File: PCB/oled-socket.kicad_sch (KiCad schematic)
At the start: 30 parts, among them IC17 TPS6734ID, J5 3-2328724-1

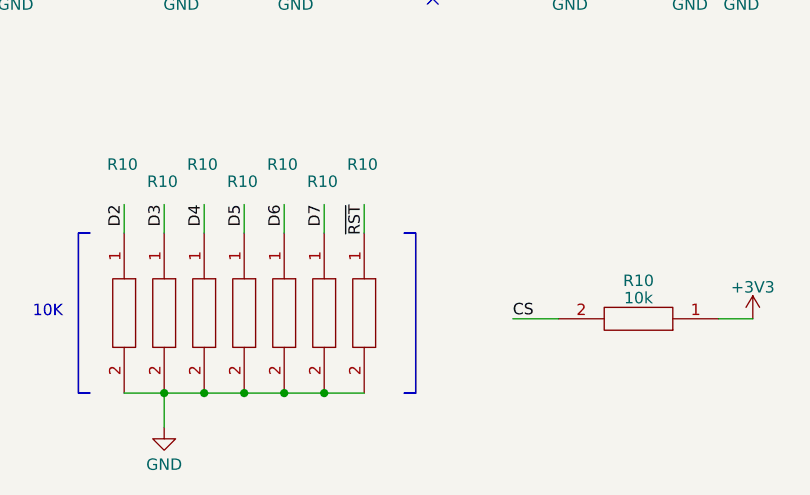
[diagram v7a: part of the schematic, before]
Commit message: redo pinout of entire MCU (closes #34)
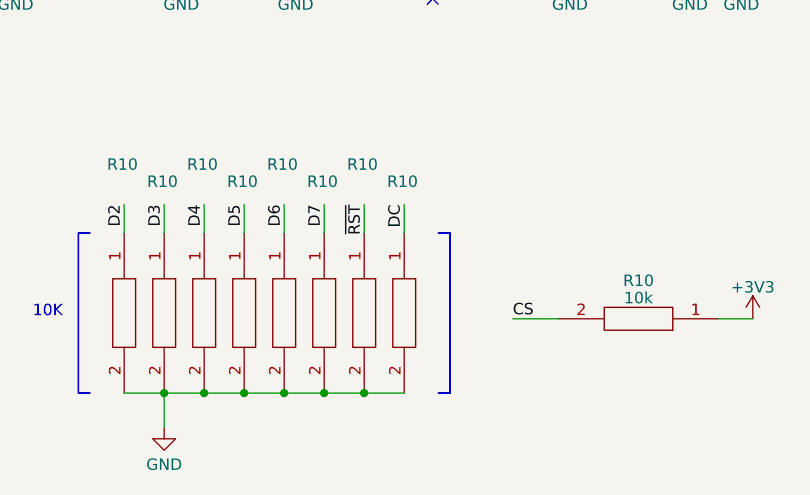
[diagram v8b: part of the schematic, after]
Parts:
- added R10: 10k, RESC1005X40N, symbol SamacSys_Parts:RK73H1ETTP1002F
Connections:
- net DC: now also R10.1
- net GND: now also R10.2
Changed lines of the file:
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@@
     (comment 2 "Joshua Lee Junon")
+  )
+  (junction (at 78.74 174.625) (diameter 0) (color 0 0 0 0)
   )
   (junction (at 65.405 174.625) (diameter 0) (color 0 0 0 0)
@@
     (stroke (width 0) (type default))
   )
+  (wire (pts (xy 83.185 153.67) (xy 83.185 156.845))
+    (stroke (width 0) (type default))
+  )
+  (wire (pts (xy 78.74 174.625) (xy 83.185 174.625))
+    (stroke (width 0) (type default))
+  )
   (wire (pts (xy 69.85 153.67) (xy 69.85 156.845))
     (stroke (width 0) (type default))
@@
     (fill (type none))
   )
-  (rectangle (start 84.455 174.625) (end 84.455 156.845)
+  (rectangle (start 88.265 174.625) (end 88.265 156.845)
     (stroke (width 0) (type default))
     (fill (type none))
   )
-  (rectangle (start 83.185 174.625) (end 84.455 174.625)
+  (rectangle (start 86.995 174.625) (end 88.265 174.625)
     (stroke (width 0) (type default))
     (fill (type none))
   )
-  (rectangle (start 83.185 156.845) (end 84.455 156.845)
+  (rectangle (start 86.995 156.845) (end 88.265 156.845)
     (stroke (width 0) (type default))
     (fill (type none))
@@
   )
   (label "SCK" (at 74.295 45.085 180) (fields_autoplaced)
+    (effects (font (size 1.27 1.27)) (justify right bottom))
+  )
+  (label "DC" (at 83.185 153.67 270) (fields_autoplaced)
     (effects (font (size 1.27 1.27)) (justify right bottom))
   )
@@
         )
       )
+    )
+  )
+  (symbol (lib_id "SamacSys_Parts:RK73H1ETTP1002F") (at 83.185 156.845 270) (unit 1)
+    (in_bom yes) (on_board yes) (dnp no)
+    (property "Reference" "R10" (at 81.28 151.13 90)
+      (effects (font (size 1.27 1.27)) (justify left))
+    )
+    (property "Value" "10k" (at 85.1662 167.0123 90)
+      (effects (font (size 1.27 1.27)) (justify left) hide)
+    )
+    (property "Footprint" "RESC1005X40N" (at 84.455 170.815 0)
+      (effects (font (size 1.27 1.27)) (justify left) hide)
+    )
+    (property "Datasheet" "http://www.koaspeer.com/catimages/Products/RK73-RT/RK73-RT.pdf" (at 81.915 170.815 0)
+      (effects (font (size 1.27 1.27)) (justify left) hide)
+    )
+    (property "Description" "Resistor,ThickFilm1005,0.063W,10kohm" (at 79.375 170.815 0)
+      (effects (font (size 1.27 1.27)) (justify left) hide)
+    )
+    (property "Height" "0.4" (at 76.835 170.815 0)
+      (effects (font (size 1.27 1.27)) (justify left) hide)
+    )
+    (property "Manufacturer_Name" "KOA Speer" (at 74.295 170.815 0)
+      (effects (font (size 1.27 1.27)) (justify left) hide)
+    )
+    (property "Manufacturer_Part_Number" "RK73H1ETTP1002F" (at 71.755 170.815 0)
+      (effects (font (size 1.27 1.27)) (justify left) hide)
+    )
+    (property "Mouser Part Number" "660-RK73H1ETTP1002F" (at 69.215 170.815 0)
+      (effects (font (size 1.27 1.27)) (justify left) hide)
+    )
+    (property "Mouser Price/Stock" "https://www.mouser.co.uk/ProductDetail/KOA-Speer/RK73H1ETTP1002F?qs=uLfVlVfCHH2OZ4JTybrBPQ%3D%3D" (at 66.675 170.815 0)
+      (effects (font (size 1.27 1.27)) (justify left) hide)
+    )
+    (property "Arrow Part Number" "RK73H1ETTP1002F" (at 64.135 170.815 0)
+      (effects (font (size 1.27 1.27)) (justify left) hide)
+    )
+    (property "Arrow Price/Stock" "https://www.arrow.com/en/products/rk73h1ettp1002f/koa-speer-electronics?region=nac" (at 61.595 170.815 0)
+      (effects (font (size 1.27 1.27)) (justify left) hide)
+    )
+    (property "Mouser Testing Part Number" "" (at 59.055 170.815 0)
+      (effects (font (size 1.27 1.27)) (justify left) hide)
+    )
+    (property "Mouser Testing Price/Stock" "" (at 56.515 170.815 0)
+      (effects (font (size 1.27 1.27)) (justify left) hide)
+    )
+    (pin "1")
+    (pin "2")
+    (instances
+      (project "Oro Testbed v2"
+        (path "/3d0fc623-63eb-45e5-a304-e470d9b3a173"
+          (reference "R10") (unit 1)
+        )
+        (path "/3d0fc623-63eb-45e5-a304-e470d9b3a173/7310340d-2c15-4c32-b17d-f4923dae9f8e"
+          (reference "R8") (unit 1)
+        )
+      )
+      (project "OroLink"
+        (path "/e89dcd22-1250-4a5b-b778-1c95a0dd623d/1b3eede1-74b0-4c0b-b4f1-7ec1bfc1f54f"
+          (reference "R53") (unit 1)
+        )
+      )
